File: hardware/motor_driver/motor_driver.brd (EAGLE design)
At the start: 93.7 x 72.4 mm, 88 parts

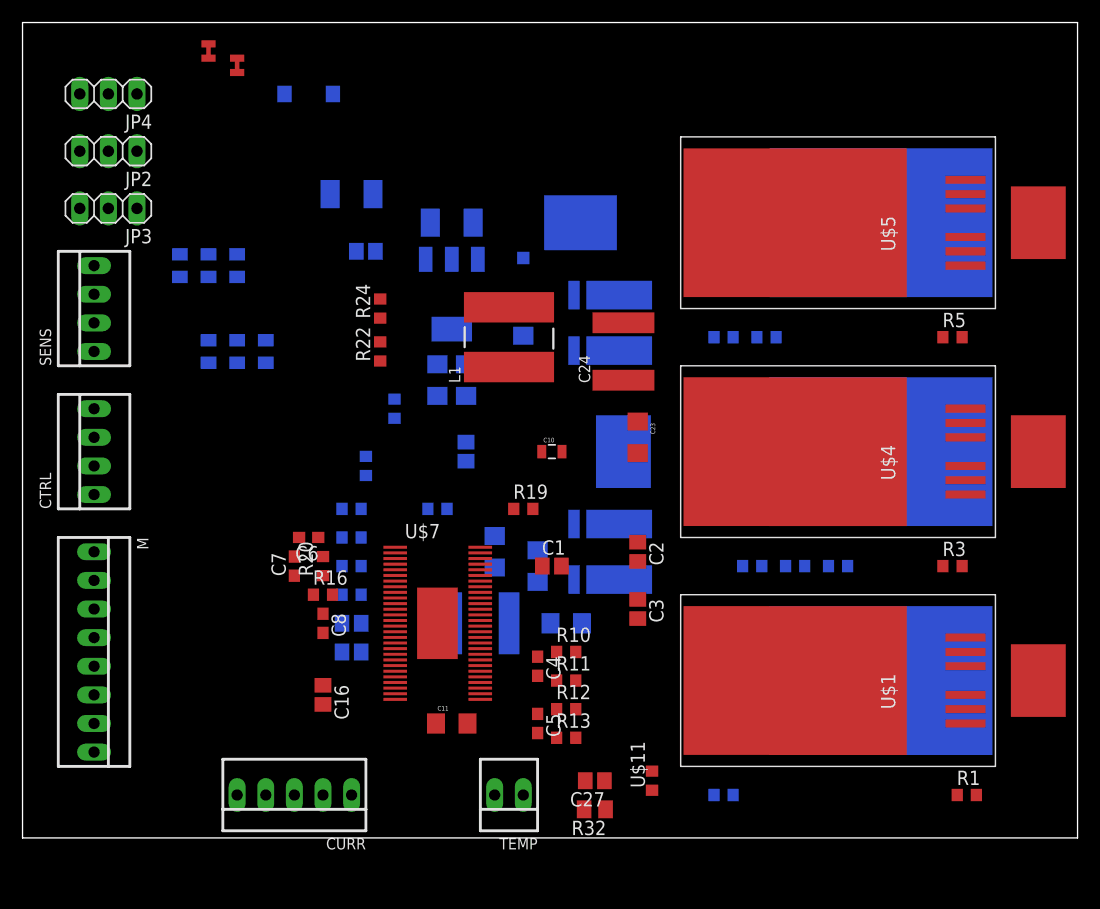
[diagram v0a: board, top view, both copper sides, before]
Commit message: Routed mosfets
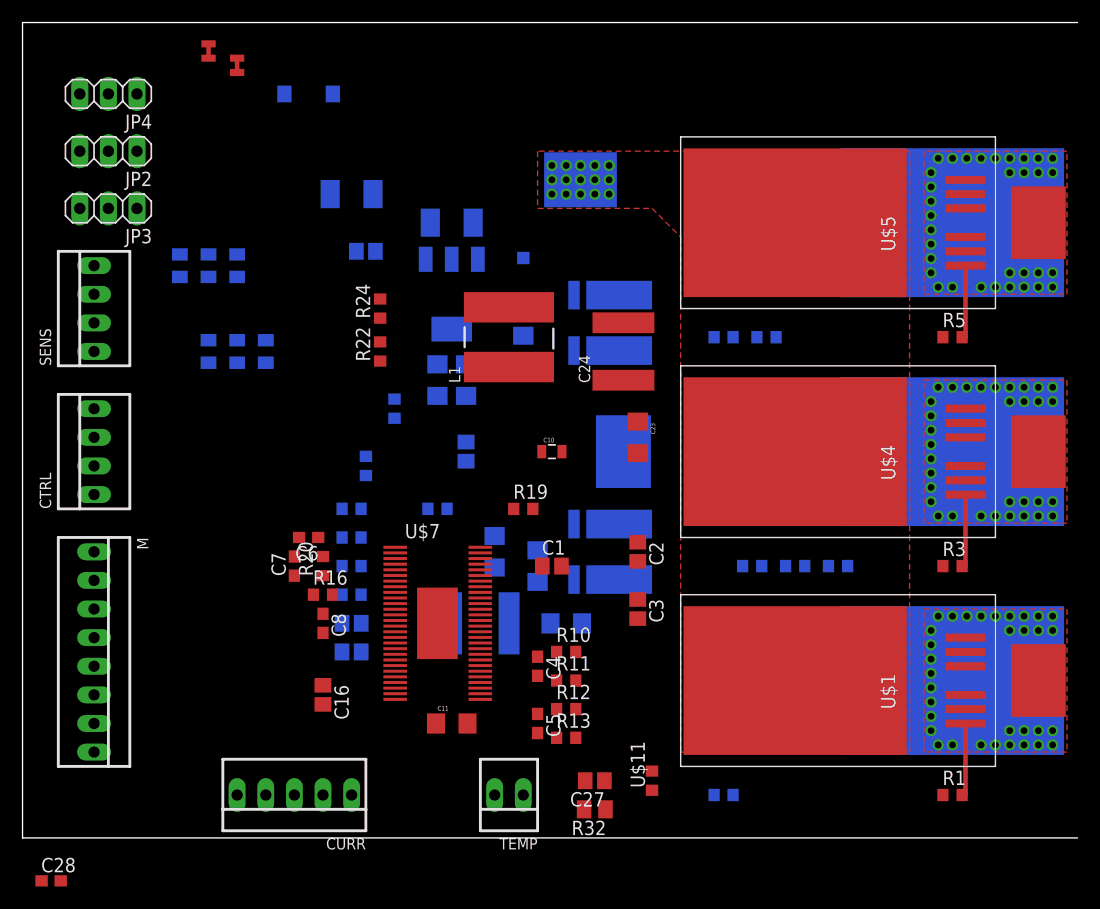
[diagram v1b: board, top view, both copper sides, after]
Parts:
- added C28: 0nF, adafruit:C0603
- C6: value 6.8nF -> 120pF
- C7: value 120pF -> 6.8nF
- moved U$2 6.35 mm to (87.6, 14.0)
- moved U$3 6.35 mm to (87.6, 34.3)
- moved U$6 6.35 mm to (87.6, 54.6)
- moved U$15 3.81 mm to (55.9, 58.4)
- moved R1 1.27 mm to (88.9, 3.81)
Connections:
- new net N$9: C28.1, U$7.P$56
- net DGND: now also C28.2
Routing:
- net N$4: track 0.00 -> 6.66 mm
- net N$1: track 0.00 -> 6.66 mm
- net N$5: track 0.00 -> 6.66 mm
- added copper zone on layer 1, net H1_VS
- added copper zone on layer 1, net H2_VS
- added copper zone on layer 1, net H3_VS
- added copper zone on layer 1, net VCC

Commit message: more mosfet stuff
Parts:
- moved U$8 7.10 mm to (61.6, 19.1)
- moved U$9 5.85 mm to (62.9, 49.5), turned to 90 degrees
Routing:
- net N$2: track 0.00 -> 28.9 mm
- net N$6: track 0.00 -> 11.2 mm
- net N$3: track 0.00 -> 9.20 mm
- net H1_LOW: track 0.00 -> 2.11 mm
- added copper zone on layer 16, net GND
- added copper zone on layer 16, net H1_LOW
- added copper zone on layer 16, net H3_LOW
